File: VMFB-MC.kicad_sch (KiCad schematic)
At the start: 44 parts, among them J1 Conn_01x04_Pin, J10 Conn_01x04_Pin, J2 Conn_01x04_Pin, J3 Conn_01x04_Pin, J4 Conn_01x02_Pin, J5 Conn_01x03_Pin, J6 Conn_01x04_Pin, J7 Conn_01x04_Pin, J8 Conn_01x04_Pin, J9 Conn_01x05_Pin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

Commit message: more clean up
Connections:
- net EMPTY: now also R14.2; no longer R14.1
- net GND: now also R14.1; no longer R14.2
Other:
- moved on the sheet: R14
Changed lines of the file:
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@@
     )
   )
-  (symbol (lib_id "Device:R") (at 139.7 101.6 90) (unit 1)
+  (symbol (lib_id "Device:R") (at 139.7 101.6 270) (mirror x) (unit 1)
     (in_bom yes) (on_board yes) (dnp no)
     (property "Reference" "R14" (at 139.7 104.14 90)

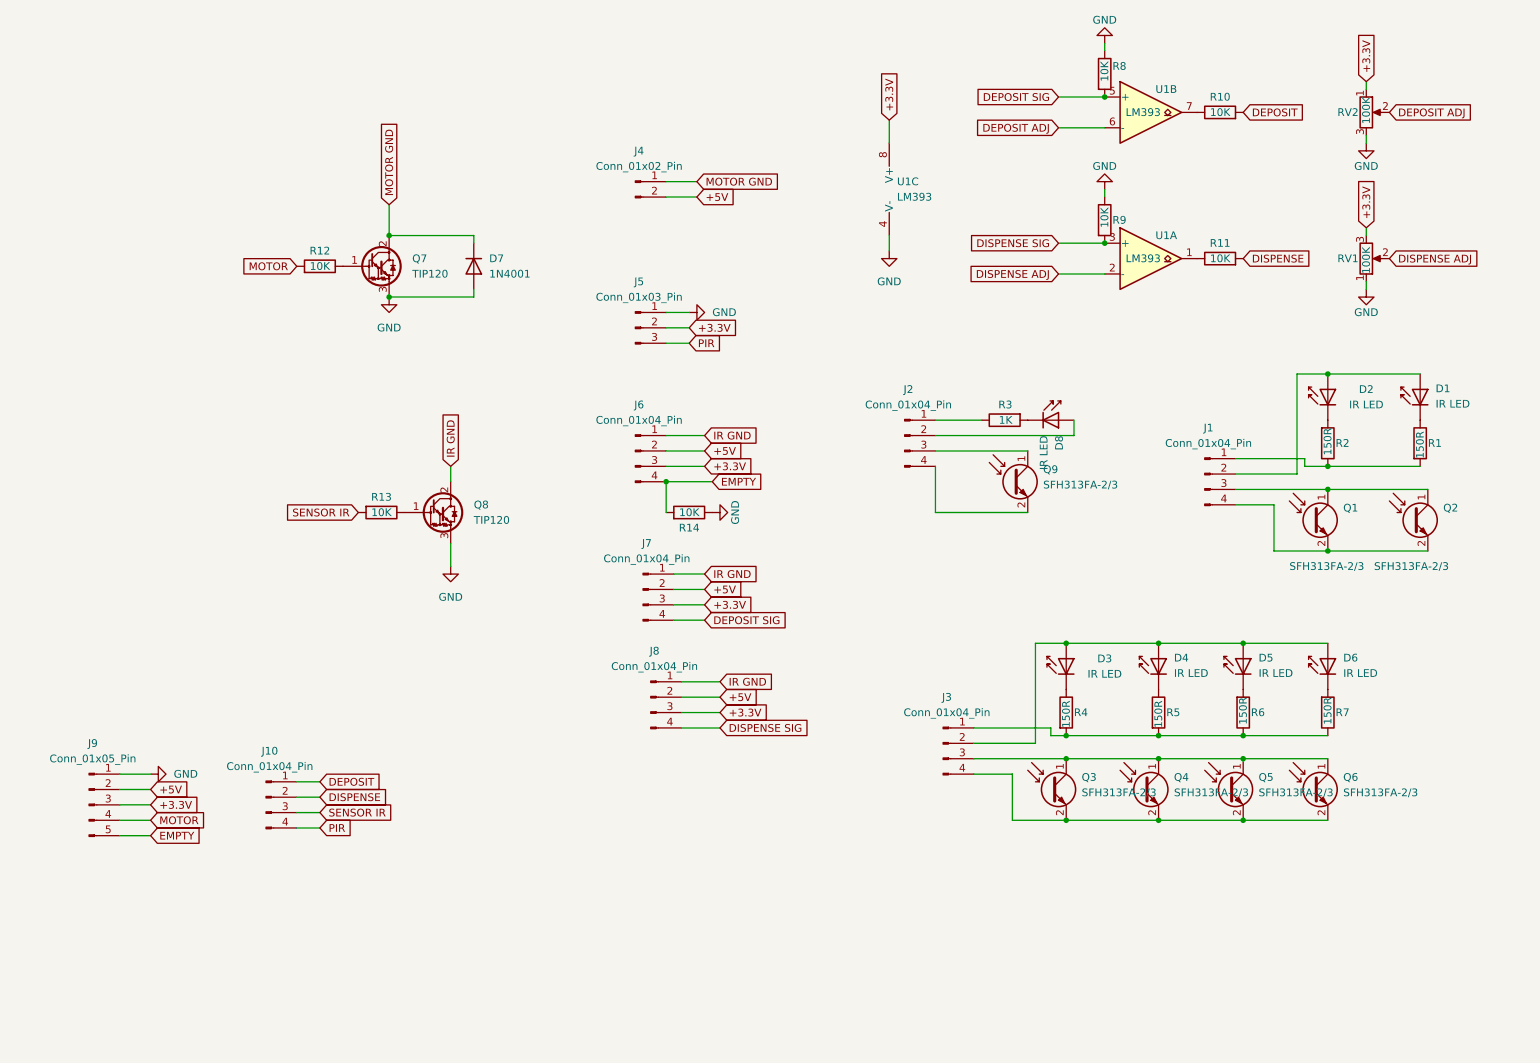
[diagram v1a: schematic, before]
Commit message: better schematic labelling
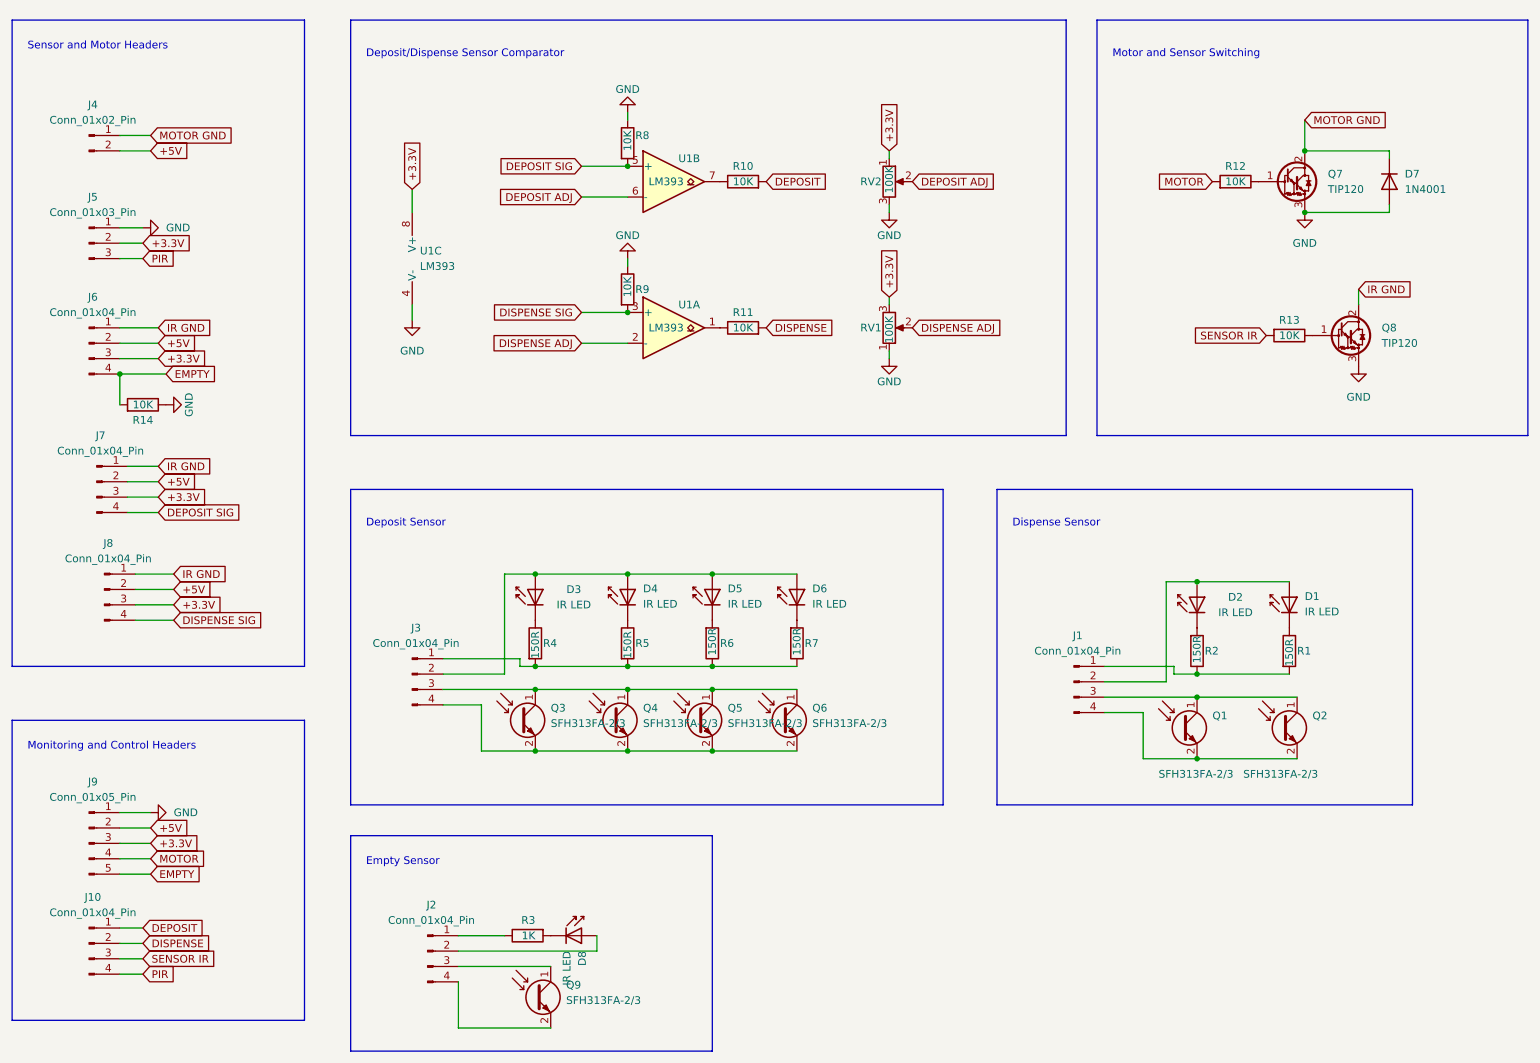
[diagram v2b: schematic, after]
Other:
- note added: "Deposit Sensor"
- note added: "Deposit/Dispense Sensor Comparator"
- note added: "Dispense Sensor"
- note added: "Empty Sensor"
- note added: "Monitoring and Control Headers"
- note added: "Motor and Sensor Switching"
- note added: "Sensor and Motor Headers"
- moved on the sheet: D1, D2, D3, D4, D5, D6, D7, D8, J1, J10, J2, J3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

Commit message: schematic labelling
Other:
- note added: "3V3"
- note added: "5V"
- note added: "IR GND"
- note added: "SIG"
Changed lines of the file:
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@@
+    (effects (font (size 1.27 1.27)) (justify left bottom))
+  )
+  (text "IR GND" (at 86.36 127 0)
     (effects (font (size 1.27 1.27)) (justify left bottom))
   )
@@
     (effects (font (size 1.27 1.27)) (justify left bottom))
   )
+  (text "3V3" (at 195.58 133.35 0)
+    (effects (font (size 1.27 1.27)) (justify left bottom))
+  )
+  (text "5V" (at 195.58 130.81 0)
+    (effects (font (size 1.27 1.27)) (justify left bottom))
+  )
+  (text "IR GND" (at 88.9 172.72 0)
+    (effects (font (size 1.27 1.27)) (justify left bottom))
+  )
+  (text "5V" (at 88.9 175.26 0)
+    (effects (font (size 1.27 1.27)) (justify left bottom))
+  )
+  (text "IR GND" (at 195.58 128.27 0)
+    (effects (font (size 1.27 1.27)) (justify left bottom))
+  )
   (text "Motor and Sensor Switching" (at 209.55 26.67 0)
     (effects (font (size 1.27 1.27)) (justify left bottom))
   )
+  (text "SIG" (at 195.58 135.89 0)
+    (effects (font (size 1.27 1.27)) (justify left bottom))
+  )
   (text "Deposit Sensor" (at 86.36 104.14 0)
+    (effects (font (size 1.27 1.27)) (justify left bottom))
+  )
+  (text "3V3" (at 88.9 177.8 0)
+    (effects (font (size 1.27 1.27)) (justify left bottom))
+  )
+  (text "3V3" (at 86.36 132.08 0)
+    (effects (font (size 1.27 1.27)) (justify left bottom))
+  )
+  (text "SIG" (at 88.9 180.34 0)
     (effects (font (size 1.27 1.27)) (justify left bottom))
   )
@@
     (effects (font (size 1.27 1.27)) (justify left bottom))
   )
+  (text "SIG" (at 86.36 134.62 0)
+    (effects (font (size 1.27 1.27)) (justify left bottom))
+  )
+  (text "5V" (at 86.36 129.54 0)
+    (effects (font (size 1.27 1.27)) (justify left bottom))
+  )
